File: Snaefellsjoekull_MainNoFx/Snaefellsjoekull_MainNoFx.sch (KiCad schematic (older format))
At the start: 28 parts, among them J1 Eurorack Power, J2 Bus Connector, J3 Right Out, J4 Left Out, U1 TL072, U2 TL072

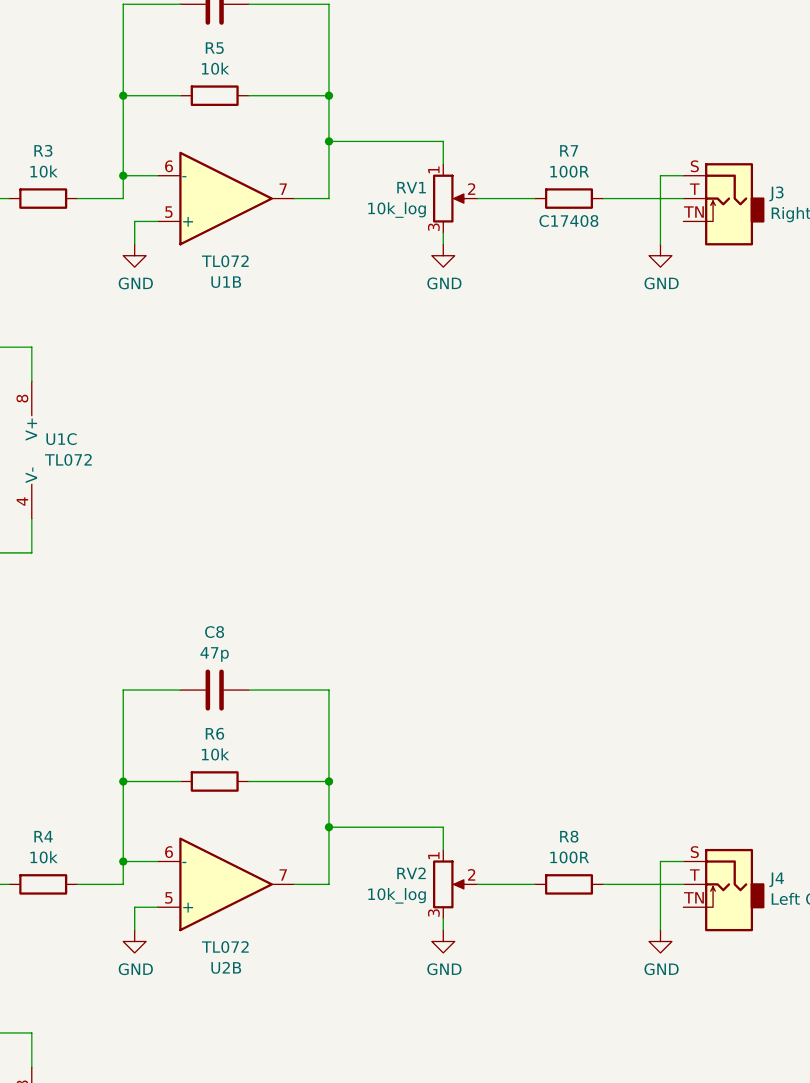
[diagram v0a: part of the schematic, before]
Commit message: Potentiometer fixed
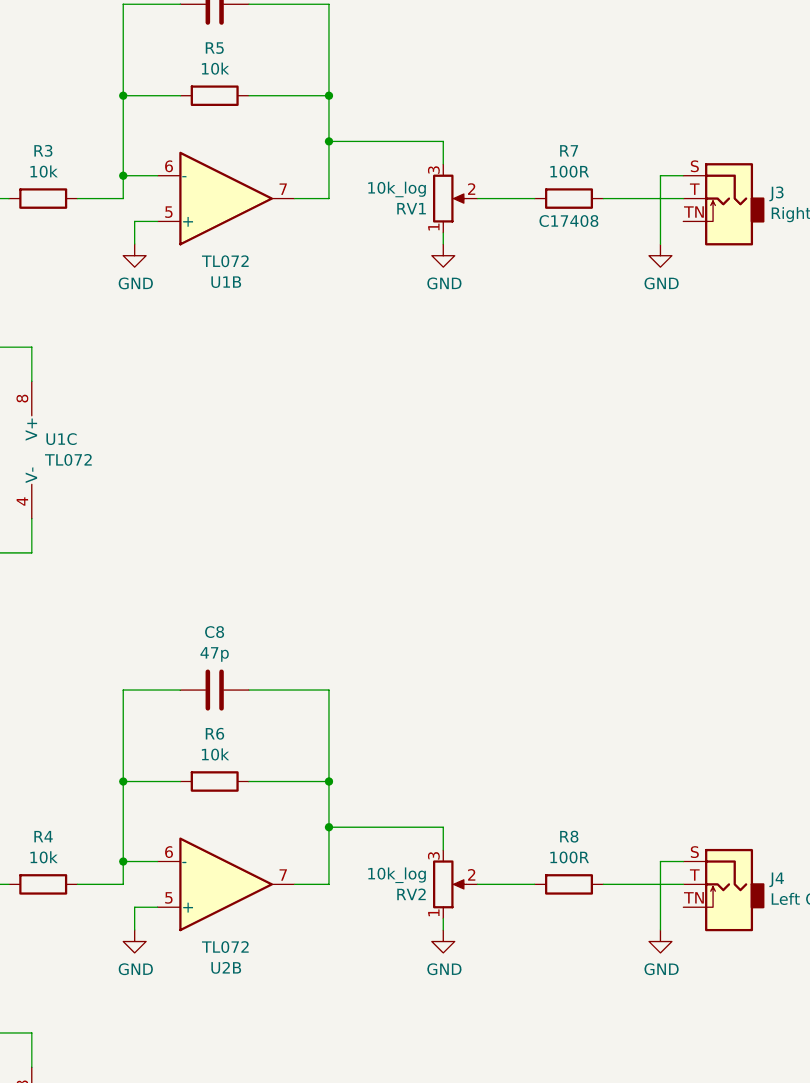
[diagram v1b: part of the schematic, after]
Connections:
- net GND: now also RV1.1, RV2.1; no longer RV1.3, RV2.3
- net at C7.2, R5.1, U1.7: now also RV1.3; no longer RV1.1
- net at C8.2, R6.1, U2.7: now also RV2.3; no longer RV2.1
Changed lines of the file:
@@
 F 3 "~" H 7800 2100 50  0001 C CNN
 	1    7800 2100
-	1    0    0    -1
+	1    0    0    1
 $EndComp
 $Comp
@@
 F 3 "~" H 7800 5100 50  0001 C CNN
 	1    7800 5100
-	1    0    0    -1
-$EndComp
-$Comp
+	1    0    0    1
+$EndComp
+$Comp
